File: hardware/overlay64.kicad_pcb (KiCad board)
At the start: 2 copper layers, 44.5 x 58.4 mm, 26 parts, among them IC1 ATMEGA1284, P1 USB, P2 INPUT, P3 CONTROL, P4 MAIN, P5 HOLE, P6 HOLE, P7 HOLE, P8 HOLE, P9 BYPASS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

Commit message: SMD rework
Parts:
- removed P1: USB, custom:USB-MINI-B-TH
- removed SW1: SW_BOOT, custom:Button
- added J1: USB_B_Mini, Connector_USB:USB_Mini-B_Lumberg_2486_01_Horizontal, F.Cu at (130.0, 115.1)
- IC1: value ATMEGA1284 -> ATmega1284P-AU; footprint Housings_DIP:DIP-40_W15.24mm -> Package_QFP:TQFP-44_10x10mm_P0.8mm
- R1, R2, R3: footprint Discret:R3 -> Resistor_SMD:R_0805_2012Metric_Pad1.15x1.40mm_HandSolder
- moved IC1 25.1 mm to (145.5, 87.1)
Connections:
- IC1 pad 1: /~HSYNC -> /MOSI
- IC1 pad 10: VCC -> Net-(IC1-Pad10)
- IC1 pad 11: GND -> Net-(IC1-Pad11)
- IC1 pad 12: Net-(C2-Pad2) -> /~VSYNC
- IC1 pad 13: Net-(C3-Pad2) -> /C6
- IC1 pad 14: /BOOT -> /C7
- IC1 pad 15: Net-(IC1-Pad15) -> /C0
- IC1 pad 16: Net-(IC1-Pad16) -> /C1
- IC1 pad 17: /~VSYNC -> VCC
- IC1 pad 18: /C6 -> GND
- IC1 pad 19: /C7 -> /IN15
- IC1 pad 2: /C2 -> /C4
- IC1 pad 20: /C0 -> /IN14
- IC1 pad 21: /C1 -> /IN13
- IC1 pad 22: /IN15 -> /IN12
- IC1 pad 23: /IN14 -> /IN11
- IC1 pad 24: /IN13 -> /IN10
- IC1 pad 25: /IN12 -> /IN9
- IC1 pad 26: /IN11 -> /IN8
- IC1 pad 27: /IN10 -> VCC
- IC1 pad 28: /IN9 -> GND
- IC1 pad 29: /IN8 -> Net-(IC1-Pad29)
- IC1 pad 3: /~BURST -> /C5
- IC1 pad 30: VCC -> /IN7
- IC1 pad 31: GND -> /IN6
- IC1 pad 32: Net-(IC1-Pad32) -> /IN5
- IC1 pad 33: /IN7 -> /IN4
- IC1 pad 34: /IN6 -> /IN3
- IC1 pad 35: /IN5 -> /IN2
- IC1 pad 36: /IN4 -> /IN1
- IC1 pad 37: /IN3 -> /IN0
- IC1 pad 38: /IN2 -> VCC
- IC1 pad 39: /IN1 -> GND
- IC1 pad 4: /C3 -> Net-(IC1-Pad4)
- IC1 pad 40: /IN0 -> /~HSYNC
- IC1 pad 5: Net-(IC1-Pad5) -> VCC
- IC1 pad 6: /MOSI -> GND
- IC1 pad 7: /C4 -> Net-(C3-Pad2)
- IC1 pad 8: /C5 -> Net-(C2-Pad2)
- IC1 pad 9: Net-(IC1-Pad9) -> /BOOT
- R1 pad 2: Net-(IC1-Pad15) -> Net-(IC1-Pad10)
- R2 pad 2: Net-(IC1-Pad16) -> Net-(IC1-Pad11)
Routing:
- net GND: track 128.5 -> 161.1 mm, vias 0 -> 6
- net /~HSYNC: track 15.0 -> 45.1 mm, vias 0 -> 3
- net Net-(IC1-Pad10): track 0.00 -> 29.5 mm, vias 0 -> 2
- net /C2: track 53.4 -> 81.9 mm, vias 0 -> 2
- net Net-(IC1-Pad11): track 0.00 -> 27.9 mm, vias 0 -> 2
- net VCC: track 85.9 -> 112.3 mm, vias 0 -> 1
- net /IN12: track 73.0 -> 48.8 mm, vias 0 -> 1
- net /C0: track 3.81 -> 25.6 mm
- net /BOOT: track 19.9 -> 39.0 mm, vias 0 -> 4
- net /IN0: track 41.8 -> 59.1 mm
- net /C3: track 47.6 -> 64.4 mm, vias 0 -> 4
- net /IN13: track 39.4 -> 54.6 mm
- net /IN1: track 42.4 -> 56.7 mm
- net /IN14: track 38.9 -> 53.1 mm, vias 0 -> 1
- net Net-(C2-Pad2): track 8.66 -> 21.9 mm, vias 0 -> 1
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
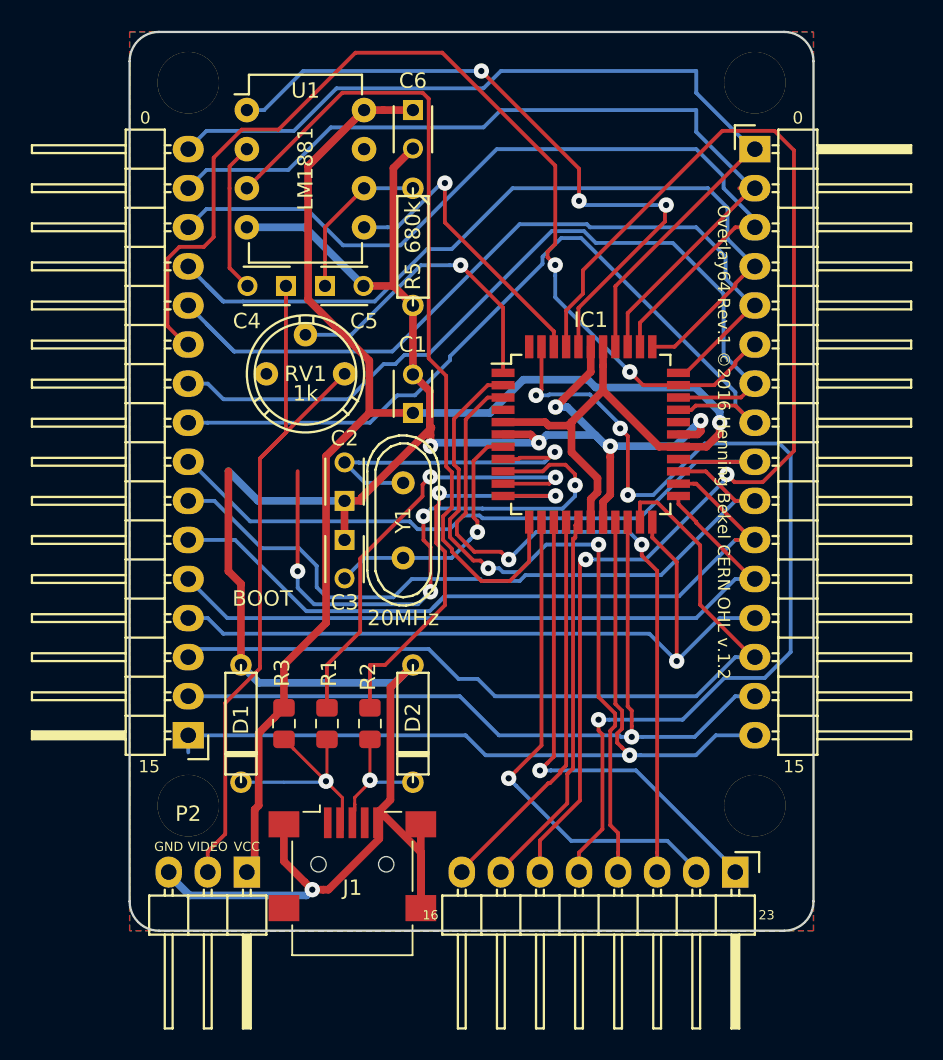
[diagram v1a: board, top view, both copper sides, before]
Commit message: Add logos
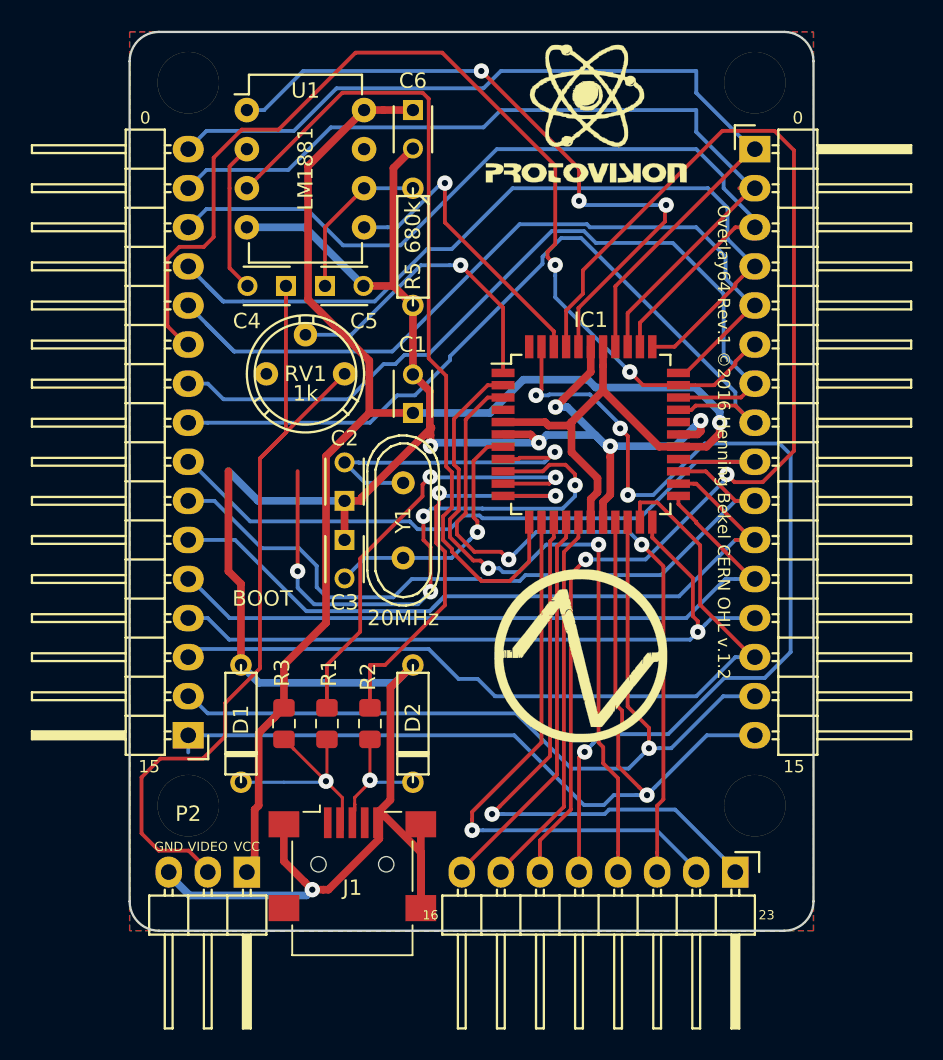
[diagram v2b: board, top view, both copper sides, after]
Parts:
- added G***: LOGO, custom:phol-labs_neg2, F.Cu at (144.9, 101.5)
- added G***: LOGO, custom:ptv_k_fsl, F.Cu at (145.2, 66.2)
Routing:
- net /LUMA: track 49.0 -> 55.3 mm
- net /C7: track 32.2 -> 38.5 mm
- net /IN15: track 54.8 -> 60.5 mm
- net /C6: track 32.3 -> 37.7 mm
- net /IN14: track 53.1 -> 56.0 mm
- net /IN12: track 48.8 -> 46.4 mm
- net /C3: track 64.4 -> 63.5 mm
